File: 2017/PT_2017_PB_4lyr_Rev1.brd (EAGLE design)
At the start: 162.5 x 209.5 mm, 159 parts, among them J1 APP_2POS_CONFIG12V_VERT, J2 APP_2POS_CONFIG12V_VERT, J3 APP_2POS_CONFIG12V_VERT, J4 APP_2POS_CONFIG12V_VERT, Q12 2N7002

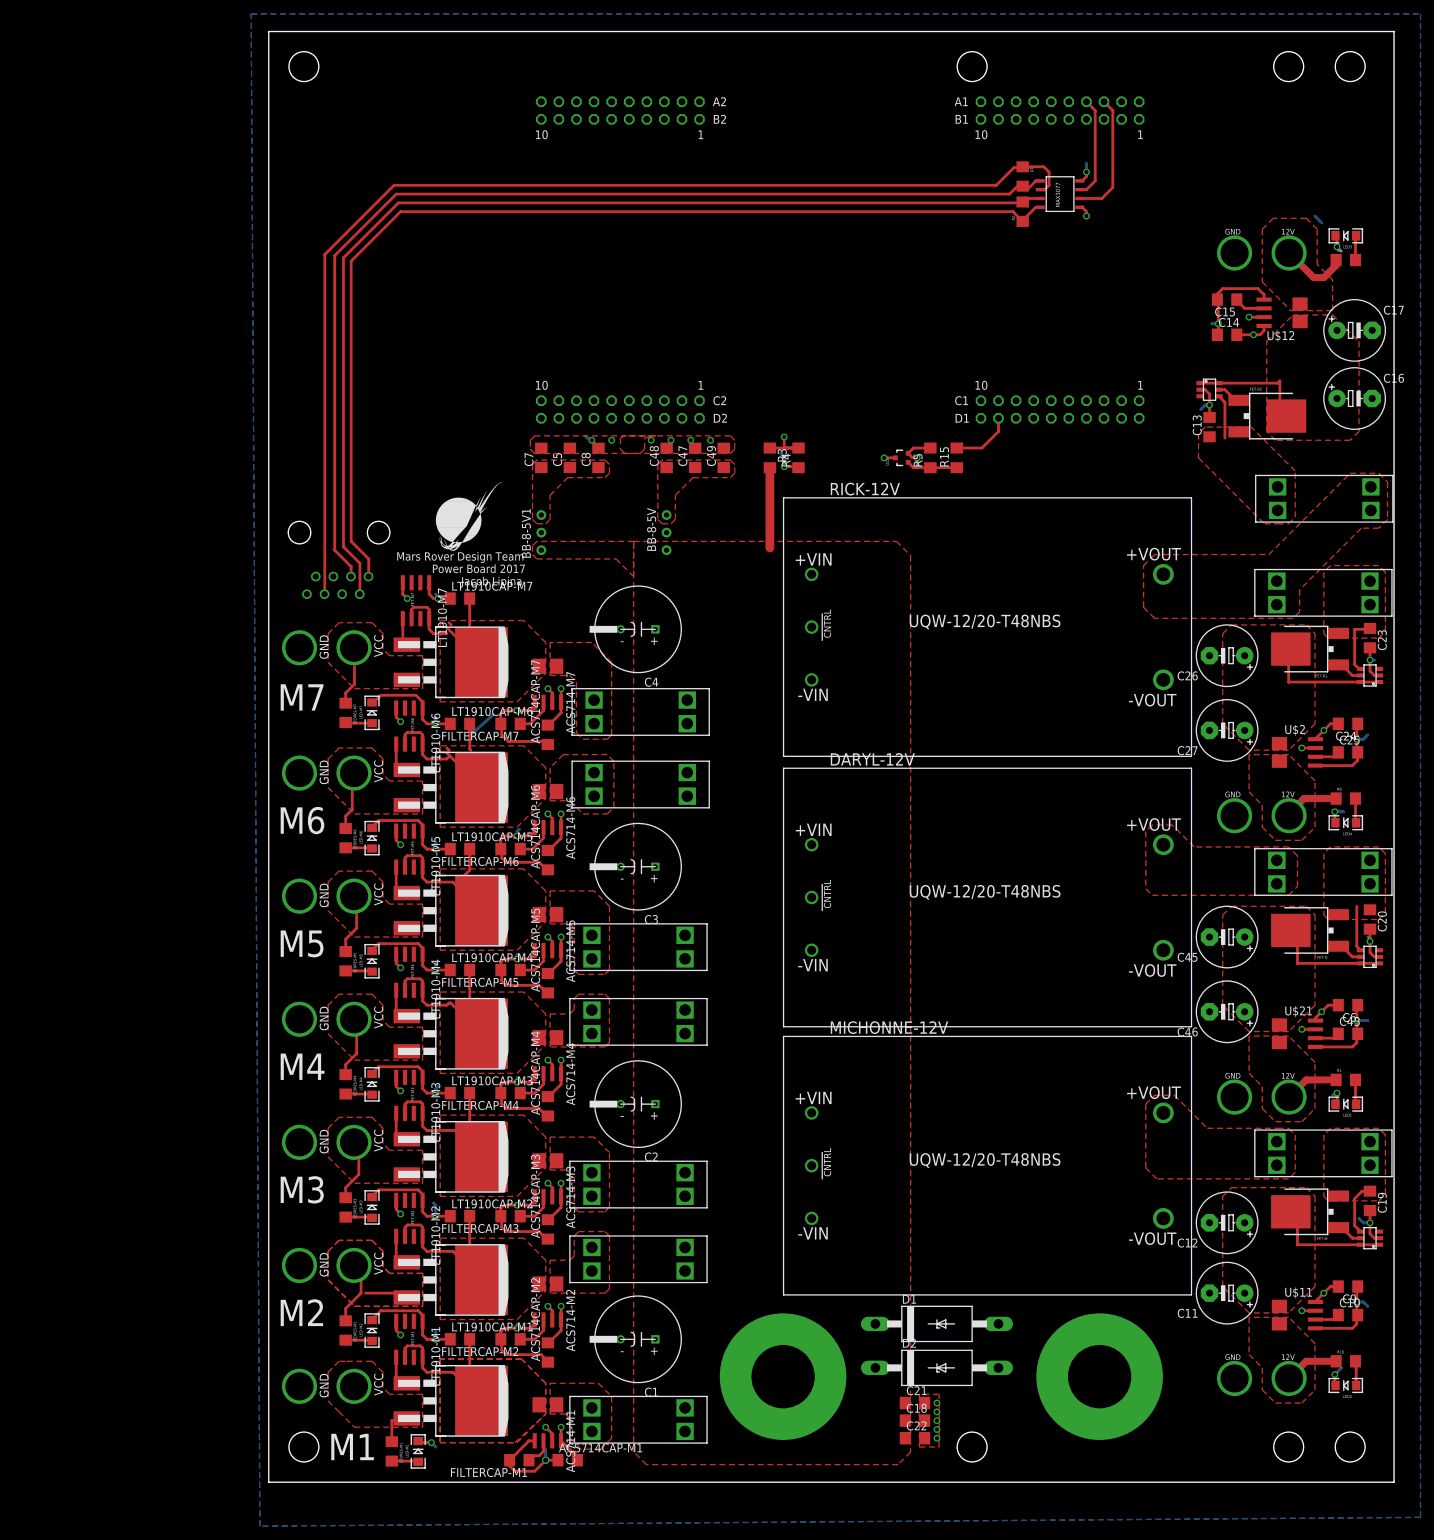
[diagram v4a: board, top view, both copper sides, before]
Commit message: Added Fan Power/Control
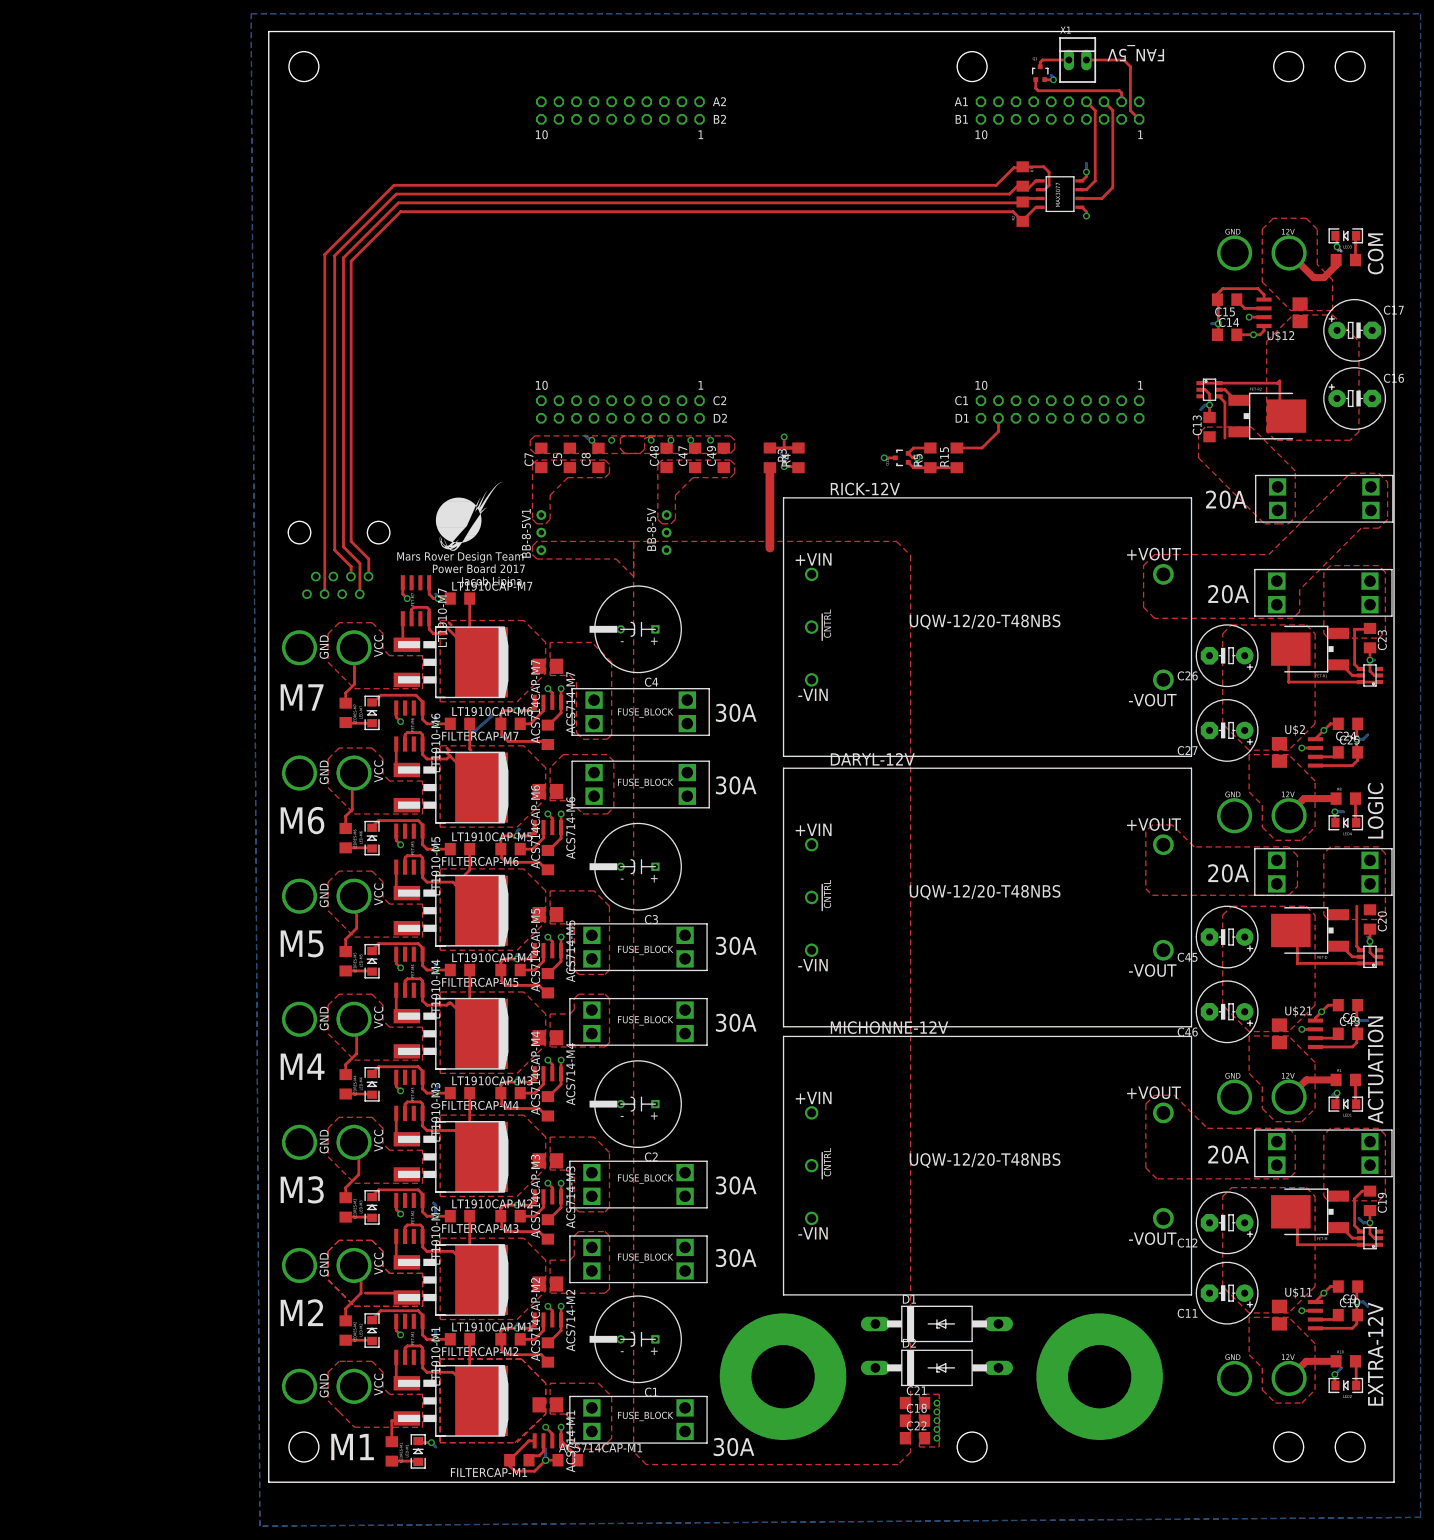
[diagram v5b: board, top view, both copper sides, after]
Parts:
- added Q1: 2N7002PW, SparkFun-DiscreteSemi:SOT323
- added X1: 22-23-2021, con-molex:22-23-2021
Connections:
- new net FAN_CTL_1: Q1.1, U$1.PE4
- new net N$66: Q1.3, X1.1
- net 5V: now also X1.2
- net GND: now also Q1.2
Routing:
- net FAN_CTL_1: track 0.00 -> 15.2 mm
- net 5V: track 151.2 -> 166.1 mm
- net N$66: track 0.00 -> 4.92 mm
- net GND: track 335.5 -> 336.2 mm, vias 41 -> 42
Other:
- board text added: "20A"
- board text added: "30A"
- board text added: "ACTUATION"
- board text added: "COM"
- board text added: "EXTRA-12V"
- board text added: "FAN_5V"
- board text added: "FUSE_BLOCK"
- board text added: "LOGIC"
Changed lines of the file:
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@@
 <layers>
 <layer number="1" name="Top" color="4" fill="1" visible="yes" active="yes"/>
-<layer number="2" name="Top-Mid(3.3)" color="10" fill="1" visible="no" active="yes"/>
+<layer number="2" name="Top-Mid(3.3)" color="10" fill="1" visible="yes" active="yes"/>
 <layer number="3" name="Route3" color="4" fill="3" visible="no" active="no"/>
 <layer number="4" name="Route4" color="1" fill="4" visible="no" active="no"/>
@@
 <layer number="13" name="Route13" color="4" fill="5" visible="no" active="no"/>
 <layer number="14" name="Route14" color="1" fill="6" visible="no" active="no"/>
-<layer number="15" name="Bot-Mid(sig)" color="14" fill="1" visible="no" active="yes"/>
+<layer number="15" name="Bot-Mid(sig)" color="14" fill="1" visible="yes" active="yes"/>
 <layer number="16" name="Bottom-GND" color="1" fill="1" visible="yes" active="yes"/>
 <layer number="17" name="Pads" color="11" fill="1" visible="yes" active="yes"/>
@@
 <layer number="113" name="IDFDebug" color="4" fill="1" visible="yes" active="yes"/>
 <layer number="114" name="Badge_Outline" color="7" fill="1" visible="no" active="yes"/>
-<layer number="115" name="ReferenceISLANDS" color="7" fill="1" visible="no" active="yes"/>
+<layer number="115" name="ReferenceISLANDS" color="7" fill="1" visible="yes" active="yes"/>
 <layer number="116" name="Patch_BOT" color="9" fill="4" visible="yes" active="yes"/>
 <layer number="118" name="Rect_Pads" color="7" fill="1" visible="yes" active="yes"/>
@@
            Power Board 2017
                     Jacob Lipina</text>
+<text x="129.54" y="207.01" size="1.778" layer="121" rot="SR180">FAN_5V</text>
+<text x="160.9725" y="10.795" size="2.1844" layer="121" rot="R90">EXTRA-12V</text>
+<text x="160.9725" y="51.7525" size="2.1844" layer="121" rot="R90">ACTUATION</text>
+<text x="160.9725" y="92.71" size="2.1844" layer="121" rot="R90">LOGIC</text>
+<text x="160.9725" y="174.3075" size="2.1844" layer="121" rot="R90">COM</text>
+<text x="141.605" y="48.5775" size="2.54" layer="121" rot="R180">20A</text>
+<text x="141.605" y="89.2175" size="2.54" layer="121" rot="R180">20A</text>
+<text x="141.605" y="129.54" size="2.54" layer="121" rot="R180">20A</text>
+<text x="141.2875" y="143.1925" size="2.54" layer="121" rot="R180">20A</text>
+<text x="70.485" y="112.395" size="2.54" layer="121" rot="R180">30A</text>
+<text x="70.485" y="101.9175" size="2.54" layer="121" rot="R180">30A</text>
+<text x="70.485" y="78.74" size="2.54" layer="121" rot="R180">30A</text>
+<text x="70.485" y="67.6275" size="2.54" layer="121" rot="R180">30A</text>
+<text x="70.485" y="44.1325" size="2.54" layer="121" rot="R180">30A</text>
+<text x="70.485" y="33.655" size="2.54" layer="121" rot="R180">30A</text>
+<text x="70.1675" y="6.35" size="2.54" layer="121" rot="R180">30A</text>
+<text x="58.42" y="10.16" size="1.016" layer="121" rot="R180">FUSE_BLOCK</text>
+<text x="58.42" y="33.02" size="1.016" layer="121" rot="R180">FUSE_BLOCK</text>
+<text x="58.42" y="44.45" size="1.016" layer="121" rot="R180">FUSE_BLOCK</text>
+<text x="58.42" y="67.31" size="1.016" layer="121" rot="R180">FUSE_BLOCK</text>
+<text x="58.42" y="77.47" size="1.016" layer="121" rot="R180">FUSE_BLOCK</text>
+<text x="58.42" y="101.6" size="1.016" layer="121" rot="R180">FUSE_BLOCK</text>
+<text x="58.42" y="111.76" size="1.016" layer="121" rot="R180">FUSE_BLOCK</text>
 </plain>
 <attributes>
@@
 <classes>
 <class number="0" name="default" width="0" drill="0">
+<clearance class="0" value="0.205"/>
 </class>
 </classes>
@@
 <element name="U$5" library="MRDT-Hardware" package="#8_SCREW" value="MOUNTING_HOLE#8" x="147.32" y="5.08"/>
 <element name="U$16" library="MRDT-Hardware" package="#8_SCREW" value="MOUNTING_HOLE#8" x="147.32" y="204.47"/>
+<element name="Q1" library="SparkFun-DiscreteSemi" package="SOT323" value="2N7002PW" x="111.4425" y="203.5175">
+<attribute name="PROD_ID" value="TRANS-11151" x="107.6325" y="220.0275" size="1.778" layer="27" display="off"/>
+</element>
+<element name="X1" library="con-molex" package="22-23-2021" value="22-23-2021" x="116.84" y="205.4225">
+<attribute name="OC_NEWARK" value="25C3832" x="105.41" y="216.8525" size="1.778" layer="27" display="off"/>
+<attribute name="MPN" value="22-23-2021" x="105.41" y="216.8525" size="1.778" layer="27" display="off"/>
+<attribute name="MF" value="MOLEX" x="105.41" y="216.8525" size="1.778" layer="27" display="off"/>
+<attribute name="OC_FARNELL" value="1462926" x="105.41" y="216.8525" size="1.778" layer="27" display="off"/>
+</element>
 </elements>
 <signals>
@@
 <contactref element="U$4" pad="P$1"/>
 <contactref element="LED4" pad="C"/>
-<wire x1="152.0825" y1="181.9275" x2="151.13" y2="182.88" width="0.4064" layer="16"/>
 <wire x1="95.5675" y1="149.377" x2="93.137" y2="149.377" width="0.4064" layer="1"/>
 <wire x1="93.137" y1="149.377" x2="92.365" y2="148.605" width="0.4064" layer="1"/>
@@
 <via x="154.305" y="178.435" extent="1-16" drill="0.6"/>
 <wire x1="154.305" y1="178.435" x2="154.94" y2="177.8" width="0.4064" layer="16"/>
+<contactref element="Q1" pad="2"/>
+<wire x1="112.0925" y1="202.5925" x2="112.0925" y2="202.58" width="0.4064" layer="1"/>
+<wire x1="112.0925" y1="202.58" x2="112.0775" y2="202.565" width="0.4064" layer="1"/>
+<wire x1="112.0775" y1="202.565" x2="113.3475" y2="202.565" width="0.4064" layer="1"/>
+<via x="113.3475" y="202.565" extent="1-16" drill="0.6"/>
+<wire x1="113.3475" y1="202.565" x2="113.3475" y2="202.8825" width="0.4064" layer="16"/>
+<wire x1="113.3475" y1="202.8825" x2="113.03" y2="203.2" width="0.4064" layer="16"/>
 </signal>
 <signal name="N$46">
@@
 <vertex x="49.2125" y="147.0025"/>
 </polygon>
+<contactref element="X1" pad="2"/>
+<wire x1="118.11" y1="205.4225" x2="123.5075" y2="205.4225" width="0.4064" layer="1"/>
+<wire x1="123.5075" y1="205.4225" x2="124.46" y2="204.47" width="0.4064" layer="1"/>
+<wire x1="124.46" y1="204.47" x2="124.46" y2="198.12" width="0.4064" layer="1"/>
+<wire x1="124.46" y1="198.12" x2="125.73" y2="196.85" width="0.4064" layer="1"/>
 </signal>
 <signal name="N$1">
@@
 <contactref element="U$14" pad="IN_2"/>
 <contactref element="MICHONNE-12V" pad="8"/>
-<polygon width="0.4064" layer="1" thermals="no">
+<polygon width="0.4064" layer="1" spacing="2.54" thermals="no">
 <vertex x="147.32" y="51.1175"/>
 <vertex x="148.2725" y="50.165"/>
@@
 <wire x1="151.19" y1="24.765" x2="149.225" y2="24.765" width="0.4064" layer="1"/>
 </signal>
+<signal name="N$66">
+<contactref element="Q1" pad="3"/>
+<contactref element="X1" pad="1"/>
+<wire x1="111.4425" y1="204.4425" x2="111.4425" y2="205.105" width="0.4064" layer="1"/>
+<wire x1="111.4425" y1="205.105" x2="111.76" y2="205.4225" width="0.4064" layer="1"/>
+<wire x1="111.76" y1="205.4225" x2="115.57" y2="205.4225" width="0.4064" layer="1"/>
+</signal>
+<signal name="FAN_CTL_1">
+<contactref element="Q1" pad="1"/>
+<contactref element="U$1" pad="PE4"/>
+<wire x1="110.7925" y1="202.5925" x2="110.7925" y2="201.31" width="0.4064" layer="1"/>
+<wire x1="110.7925" y1="201.31" x2="111.125" y2="200.9775" width="0.4064" layer="1"/>
+<wire x1="111.125" y1="200.9775" x2="122.8725" y2="200.9775" width="0.4064" layer="1"/>
+<wire x1="122.8725" y1="200.9775" x2="123.19" y2="200.66" width="0.4064" layer="1"/>
+<wire x1="123.19" y1="200.66" x2="123.19" y2="199.39" width="0.4064" layer="1"/>
+</signal>
 </signals>
